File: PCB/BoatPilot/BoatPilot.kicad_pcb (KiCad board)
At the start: 2 copper layers, 40 x 40 mm, 93 parts, among them J101 battery, J102 switch, J103 SWD, J104 wind, J105 RC, J106 GPS, J107 USB_OTG, J108 failsafe, J109 SERVO1, J110 SERVO2, J111 SERVO3, J201 GPIO, J202 USB-Audio-IR, J203 Audio-UART, P101 ICT-Point, P102 ICT-Point, P103 ICT-Point, P104 ICT-Point, P105 ICT-Point, P106 ICT-Point, P107 ICT-Point, P108 ICT-Point, P109 ICT-Point, P113 ICT-Point, P119 ICT-Point, P129 ICT-Point, P130 ICT-Point, P132 ICT-Point, P133 ICT-Point, P134 ICT-Point, P135 ICT-Point, Q101 TSM3457, U101 GY-91, U102 74LVC1G97, U103 TLV75733PDBV, U104 TPS565208, U105 24LC512, U106 74LVC1G97, U108 74LVC1G97, U109 STM32F103C8Tx, Y101 8MHz

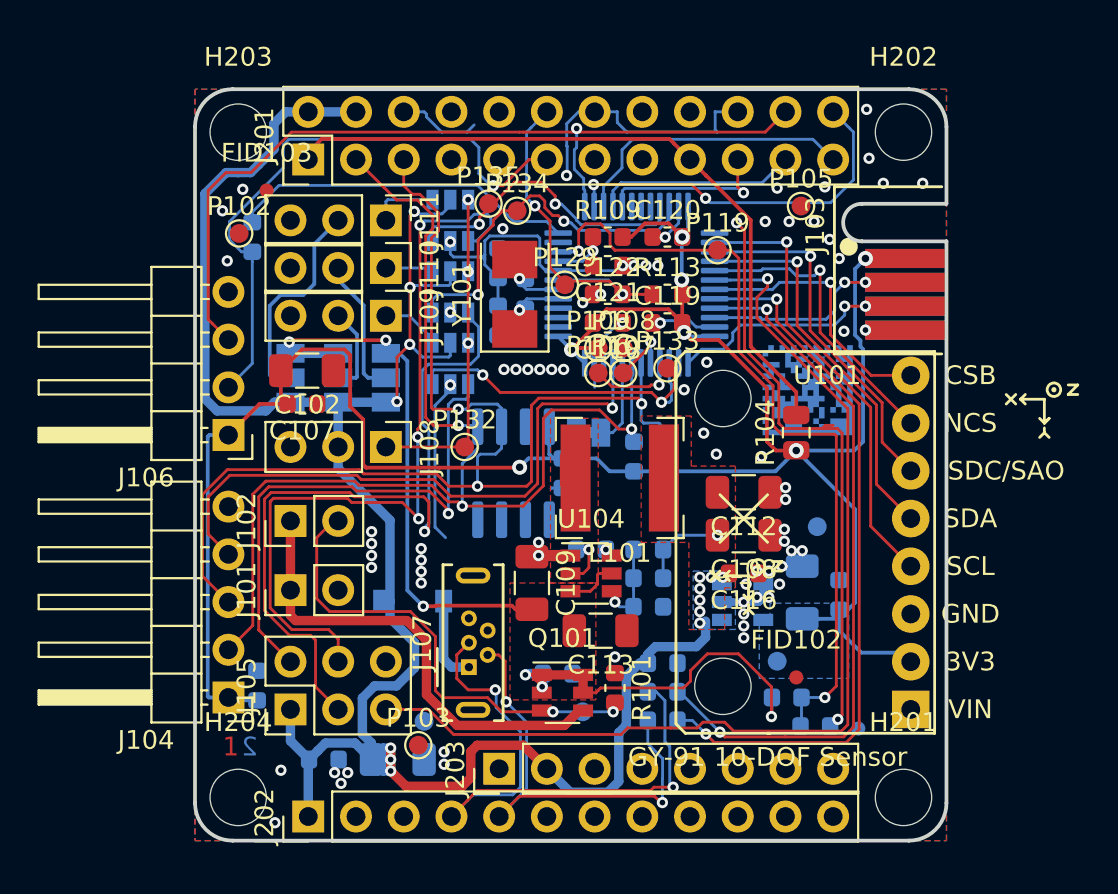
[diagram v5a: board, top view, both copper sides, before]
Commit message: Further optimize layout
Clean up the layout a bit further
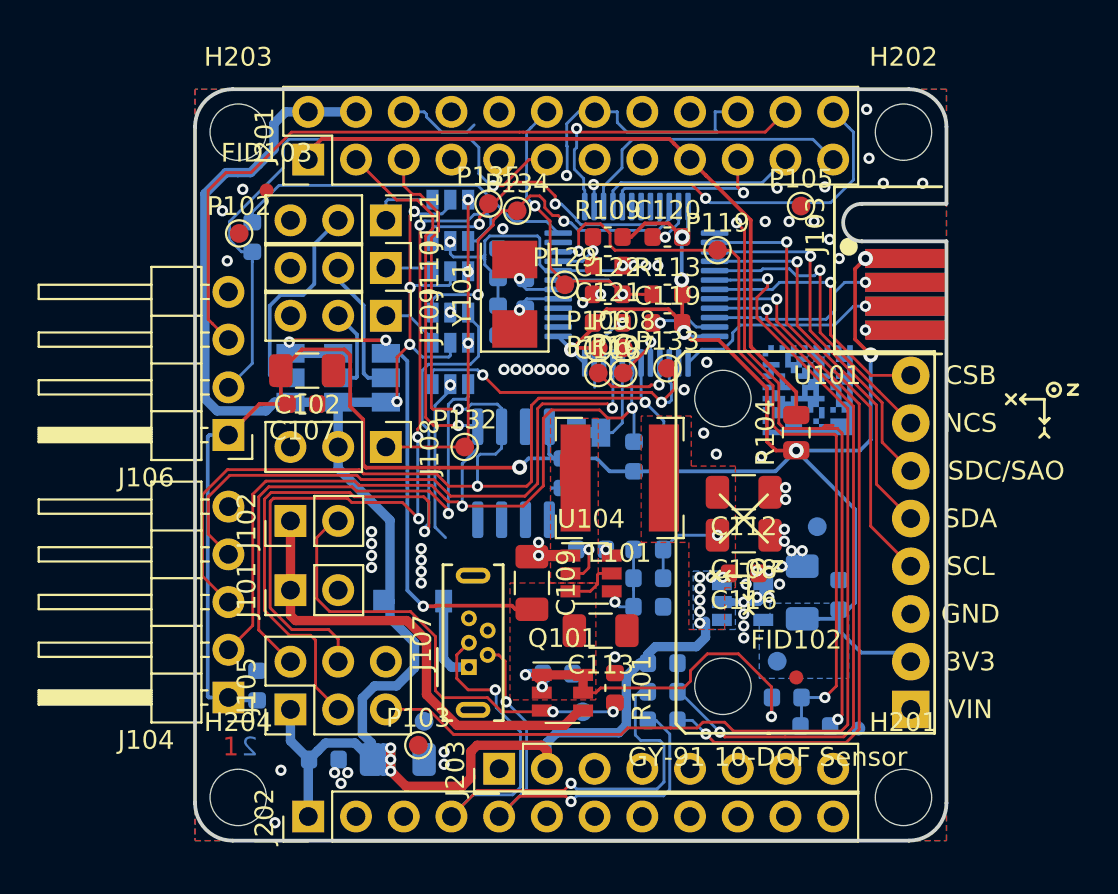
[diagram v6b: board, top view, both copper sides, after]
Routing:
- net +5V: track 124.7 -> 123.5 mm
- net /USBD+: track 34.0 -> 34.5 mm
- net +3V3: track 130.5 -> 131.1 mm, vias 7 -> 8
- net /SYS_SWCLK: track 13.4 -> 13.1 mm, vias 2 -> 1
- net GND: vias 78 -> 77
- net /SYS_SWDIO: vias 2 -> 1

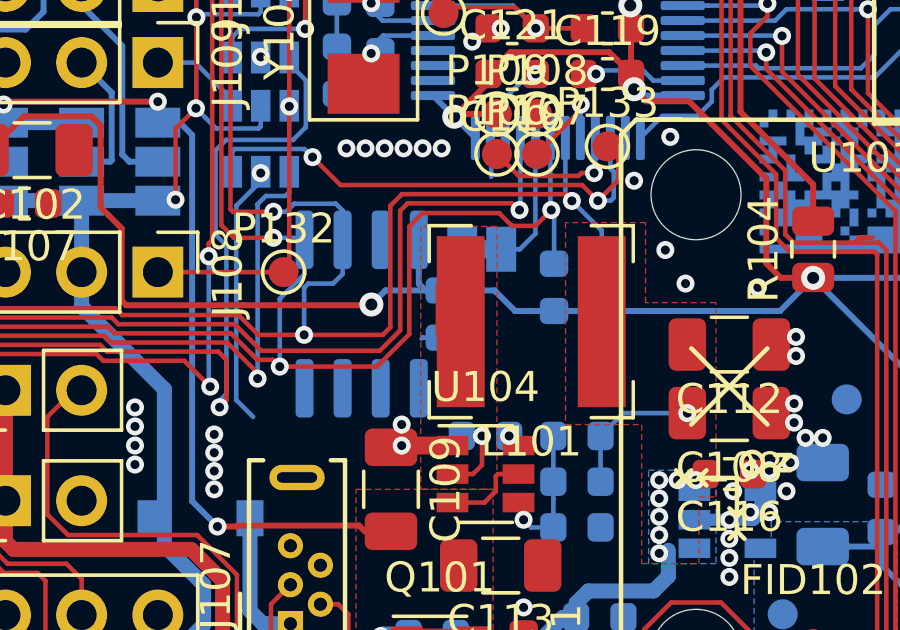
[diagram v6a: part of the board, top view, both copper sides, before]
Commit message: Shift decoupling capacitor out of eeprom IC
The capacitor was colliding with it's IC. This commit fixes the problem
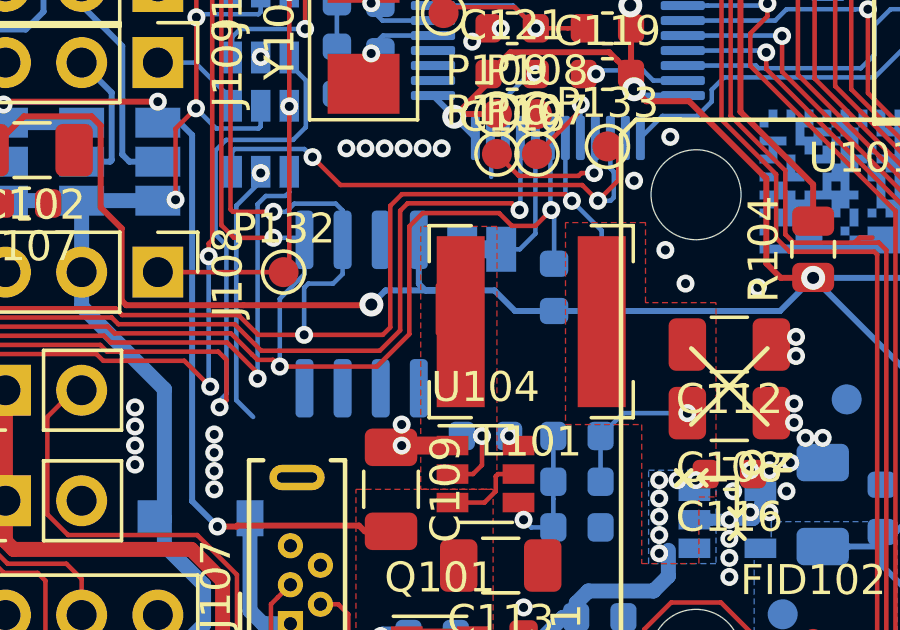
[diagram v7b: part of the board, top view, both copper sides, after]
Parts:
- moved C115 0.89 mm to (144.4, 99.5)
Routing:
- net GND: track 93.1 -> 92.5 mm
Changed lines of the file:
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@@
     (thickness 1.6)
     (drawings 16)
-    (tracks 1088)
+    (tracks 1086)
     (zones 0)
     (modules 93)
@@
     (44 Edge.Cuts user)
     (45 Margin user hide)
-    (46 B.CrtYd user hide)
+    (46 B.CrtYd user)
     (47 F.CrtYd user hide)
     (48 B.Fab user hide)
@@
   )
   (module Capacitor_SMD:C_0603_1608Metric (layer B.Cu)
-    (at 143.558 99.442 90)
+    (at 144.447 99.5055 90)
     (descr "Capacitor SMD 0603 (1608 Metric), square (rectangular) end terminal, IPC_7351 nominal, (Body size source: http://www.tortai-tech.com/upload/download/2011102023233369053.pdf), generated with kicad-footprint-generator")
     (tags capacitor)
@@
   (via (at 126.54 84.329) (size 0.6) (drill 0.3) (layers F.Cu B.Cu) (net 2))
   (via (at 140.383 86.4245) (size 0.6) (drill 0.3) (layers F.Cu B.Cu) (net 2))
-  (segment (start 143.558 100.2295) (end 142.983 100.2295) (width 0.1524) (layer B.Cu) (net 2))
-  (segment (start 142.983 100.2295) (end 142.951399 100.261101) (width 0.1524) (layer B.Cu) (net 2))
   (segment (start 143.982 103.826) (end 142.349 103.826) (width 0.6) (layer F.Cu) (net 2))
   (segment (start 142.349 103.826) (end 141.973 103.826) (width 0.6) (layer F.Cu) (net 2))
